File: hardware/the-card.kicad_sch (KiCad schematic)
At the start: 75 parts, among them J1 TYPE-C-31-M-12, J2 FH12-24S-0.5SH(55), J3 S2B-PH-SM4-TB(LF)(SN), Q1 SI2301CDS-T1-GE3, Q2 SI2301CDS-T1-GE3, Q3 SI1308EDL-T1-GE3, SW1 TS-1187A-B-A-B, SW2 TS-1187A-B-A-B, SW3 TS-1187A-B-A-B, SW4 TS-1187A-B-A-B, U1 ESP32-S3-WROOM-1-N16R8, U10 USBLC6-2SC6, U2 ST25DV04KC-IE8S3, U3 LSM6DSOTR, U4 SHT40-BD1B-R2, U5 MAX17048G+T10, U6 TP4056_C382139, U7 DW01A_C18164398, U8 8205A, U9 ME6211C33M5G-N

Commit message: feat(hardware): annotate passive relationships
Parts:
- C1: Function (none) -> MCU high-frequency supply decoupling; Related To (none) -> U1 3V3
- C10: Function (none) -> Fuel-gauge supply decoupling; Related To (none) -> U5 CELL/VDD
- C11: Function (none) -> NFC supply decoupling; Related To (none) -> U2 VCC
- C12: Function (none) -> IMU high-frequency supply decoupling; Related To (none) -> U3 VDD/VDDIO
- C13: Function (none) -> IMU local bulk capacitance; Related To (none) -> U3 VDD/VDDIO / +3V3
- C14: Function (none) -> Humidity-sensor supply decoupling; Related To (none) -> U4 VDD
- C15: Function (none) -> Addressable-LED supply decoupling; Related To (none) -> D1 VDD / AUX_3V3
- C16: Function (none) -> UP-button hardware debounce; Related To (none) -> SW1 / U1 IO4
- C17: Function (none) -> DOWN-button hardware debounce; Related To (none) -> SW2 / U1 IO5
- C18: Function (none) -> SELECT-button hardware debounce; Related To (none) -> SW3 / U1 IO6
- C19: Function (none) -> MENU-button hardware debounce; Related To (none) -> SW4 / U1 IO7
- C2: Function (none) -> MCU local bulk capacitance; Related To (none) -> U1 3V3 / +3V3
- C20: Function (none) -> E-paper switched-input bulk capacitance; Related To (none) -> J2 VCI / e-paper boost
- C21: Function (none) -> E-paper boost charge-pump capacitor; Related To (none) -> J2 / Q3 / EPD_PUMP
- C22: Function (none) -> E-paper internal core-regulator bypass; Related To (none) -> J2 VDD
- C23: Function (none) -> E-paper positive source-rail reservoir; Related To (none) -> J2 VSH2
- C24: Function (none) -> E-paper positive source-rail reservoir; Related To (none) -> J2 VSH1
- C25: Function (none) -> E-paper positive gate-rail reservoir; Related To (none) -> J2 VGH
- C26: Function (none) -> E-paper negative source-rail reservoir; Related To (none) -> J2 VSL
- C27: Function (none) -> E-paper negative gate-rail reservoir; Related To (none) -> J2 VGL
- C28: Function (none) -> E-paper common-electrode rail reservoir; Related To (none) -> J2 VCOM
- C3: Function (none) -> MCU reset and startup timing; Related To (none) -> U1 EN
- C4: Function (none) -> Battery measurement low-pass filter; Related To (none) -> U1 IO1 / battery ADC
- C5: Function (none) -> USB input bulk capacitance; Related To (none) -> J1 / U10 / U6 VBUS
- C6: Function (none) -> Charger output and battery-rail bulk capacitance; Related To (none) -> U6 BAT / +BAT
- C7: Function (none) -> Battery-protection supply decoupling; Related To (none) -> U7 VDD / BAT_NEG
- C8: Function (none) -> LDO input bypass and stability capacitance; Related To (none) -> U9 VIN
- C9: Function (none) -> LDO output stability capacitance; Related To (none) -> U9 VOUT
- R1: Function (none) -> MCU enable pull-up to +3V3; Related To (none) -> U1 EN
- R10: Function (none) -> Battery-protection pack-negative sense resistor; Related To (none) -> U7 VM / GND
- R11: Function (none) -> AUX rail P-MOSFET gate pull-up (default off); Related To (none) -> Q1 / U1 IO47
- R12: Function (none) -> E-paper P-MOSFET gate pull-up (default off); Related To (none) -> Q2 / U1 IO16
- R13: Function (none) -> Shared I2C clock pull-up; Related To (none) -> I2C_SCL / U1-U5
- R14: Function (none) -> Shared I2C data pull-up; Related To (none) -> I2C_SDA / U1-U5
- R15: Function (none) -> E-paper boost MOSFET gate pull-down; Related To (none) -> J2 GDR / Q3
- R16: Function (none) -> E-paper boost current-sense resistor; Related To (none) -> J2 RESE / Q3
- R2: Function (none) -> MCU boot-strap pull-up to +3V3; Related To (none) -> U1 IO0
- R3: Function (none) -> Battery ADC divider, upper leg; Related To (none) -> U1 IO1 / +BAT
- R4: Function (none) -> Battery ADC divider, lower leg; Related To (none) -> U1 IO1 / GND
- R5: Function (none) -> USB-C sink configuration pull-down; Related To (none) -> J1 CC1
- R6: Function (none) -> USB-C sink configuration pull-down; Related To (none) -> J1 CC2
- R7: Function (none) -> TP4056 charge-current programming (~500mA); Related To (none) -> U6 PROG
- R8: Function (none) -> Open-drain charge-status pull-up; Related To (none) -> U6 CHRG / U1 IO15
- R9: Function (none) -> Battery-protection supply feed resistor; Related To (none) -> U7 VDD / +BAT
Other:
- note added: "C1/C2 -> U1: 3V3 bypass + bulk; R1/C3 -> U1 EN: pull-up + startup timing"
- note added: "C11 -> U2: NFC bypass; R13/R14 -> I2C bus U1-U5: SCL/SDA pull-ups"
- note added: "C12/C13 -> U3: IMU bypass + bulk; C14 -> U4: sensor bypass"
- note added: "C15 -> D1: LED supply bypass"
- note added: "C16-C19 -> SW1-SW4/U1: button debounce"
- note added: "C20 -> J2 VCI: input bulk; C21 -> J2/Q3: boost pump capacitor"
- note added: "C22-C28 -> J2: core, source, gate, and VCOM rail reservoirs"
- note added: "C5 -> J1/U10/U6: USB input bulk; R5/R6 -> J1: CC1/CC2 sink pull-downs"
- note added: "C8/C9 -> U9: LDO input/output stability; C10 -> U5: fuel-gauge bypass"
- note added: "R11 -> Q1/U1: AUX gate pull-up; R12 -> Q2/U1: e-paper gate pull-up"
- note added: "R15 -> J2/Q3: boost gate pull-down; R16 -> J2/Q3: current sense"
- note added: "R2 -> U1 IO0: boot pull-up; R3/R4/C4 -> U1 IO1: battery divider + filter"
- note added: "R7 -> U6: charge-current set; R8 -> U6/U1: CHRG pull-up; C6 -> U6: BAT bulk"
- note added: "R9/R10/C7 -> U7/U8: protection supply, sense, and bypass"

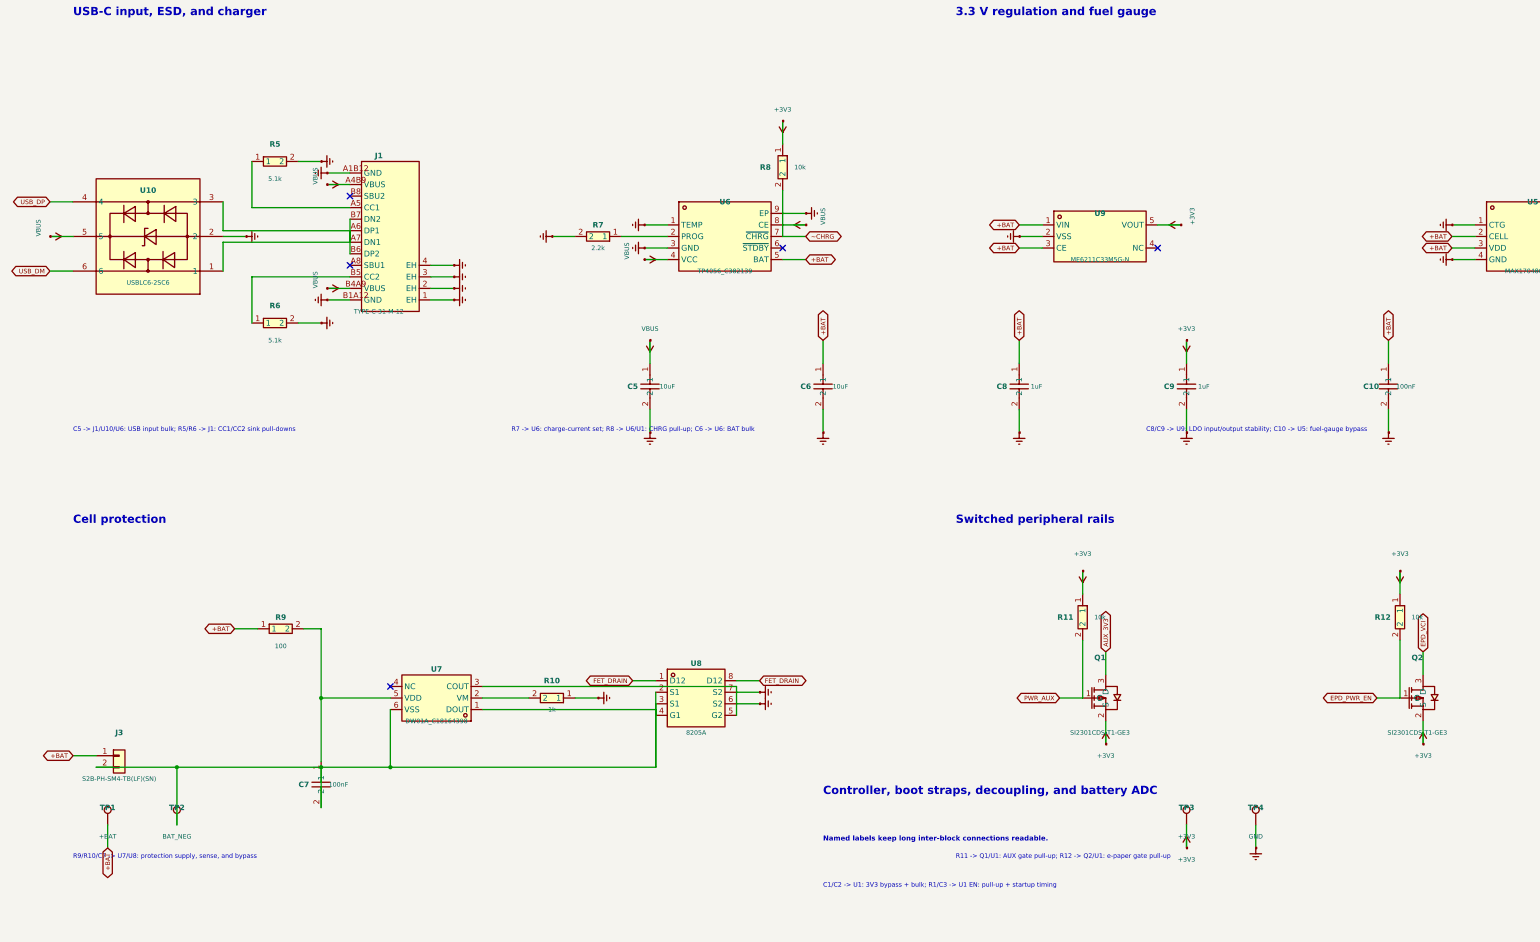
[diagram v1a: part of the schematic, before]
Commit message: feat(hardware): group schematic support passives
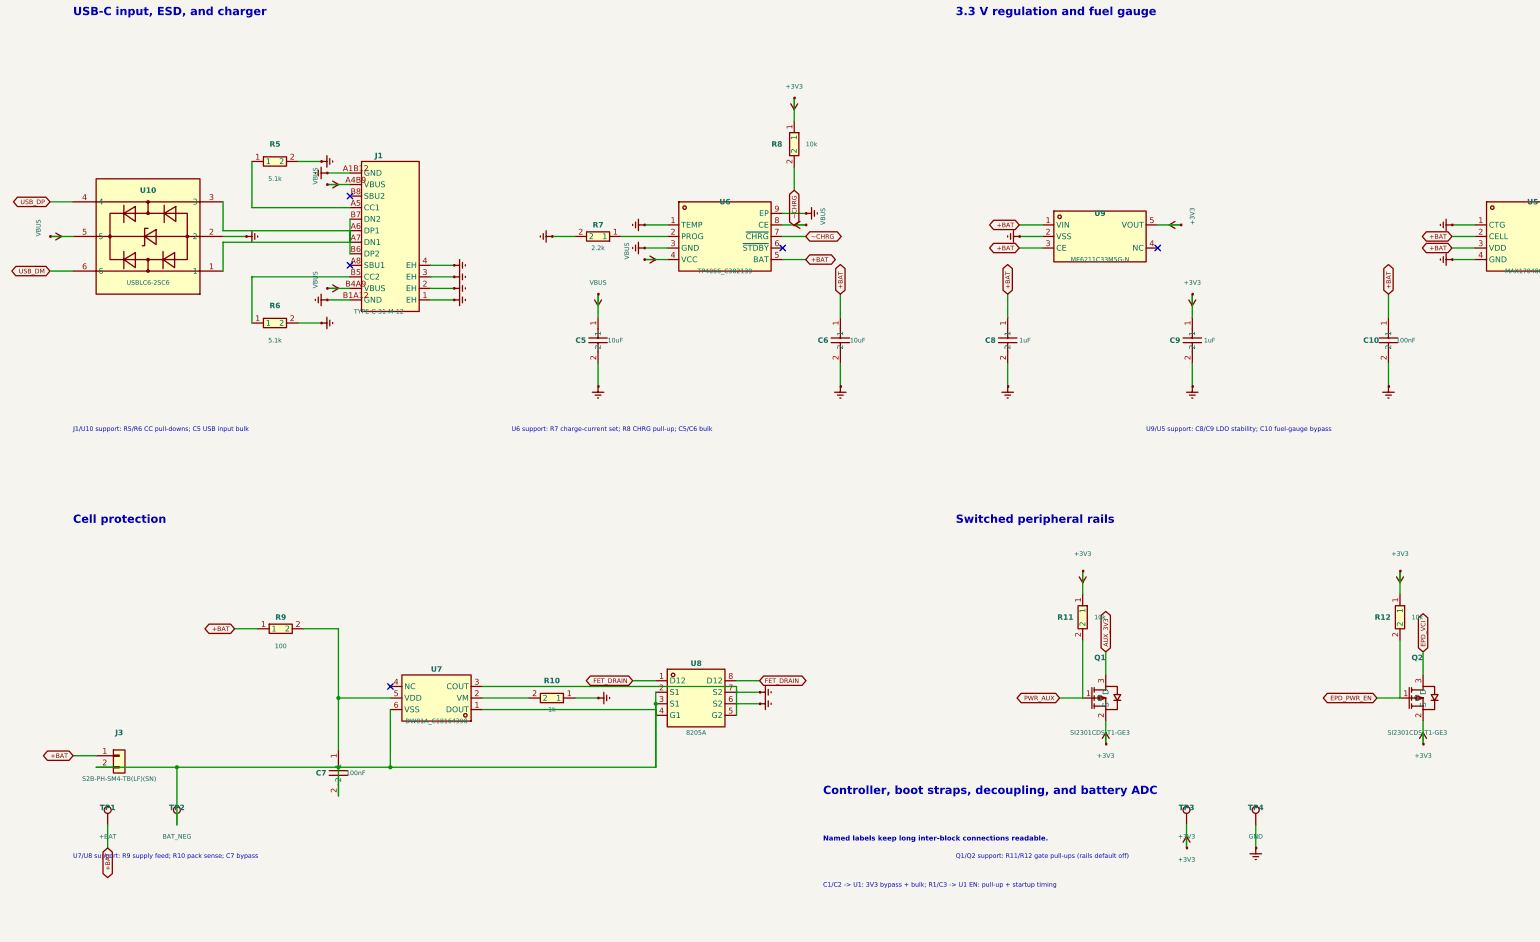
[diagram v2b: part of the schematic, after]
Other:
- note added: "J1/U10 support: R5/R6 CC pull-downs; C5 USB input bulk"
- note added: "Q1/Q2 support: R11/R12 gate pull-ups (rails default off)"
- note added: "U6 support: R7 charge-current set; R8 CHRG pull-up; C5/C6 bulk"
- note added: "U7/U8 support: R9 supply feed; R10 pack sense; C7 bypass"
- note added: "U9/U5 support: C8/C9 LDO stability; C10 fuel-gauge bypass"
- note removed: "C5 -> J1/U10/U6: USB input bulk; R5/R6 -> J1: CC1/CC2 sink pull-downs"
- note removed: "C8/C9 -> U9: LDO input/output stability; C10 -> U5: fuel-gauge bypass"
- note removed: "R11 -> Q1/U1: AUX gate pull-up; R12 -> Q2/U1: e-paper gate pull-up"
- note removed: "R7 -> U6: charge-current set; R8 -> U6/U1: CHRG pull-up; C6 -> U6: BAT bulk"
- note removed: "R9/R10/C7 -> U7/U8: protection supply, sense, and bypass"
- moved on the sheet: C10, C5, C6, C7, C8, C9, R8

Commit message: refactor(hardware): collapse local schematic labels
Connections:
- net MCU_BOOT: no longer names the net of R2.2, TP6.1, U1.27 (IO0)
- net MCU_EN: no longer names the net of C3.1, R1.2, TP5.1, U1.3 (EN)
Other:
- moved on the sheet: R8
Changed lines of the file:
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@@
 	(symbol
 		(lib_id "passives:0402WGF1002TCE")
-		(at 173.99 43.18 270)
+		(at 187.96 63.5 180)
 		(unit 1)
 		(exclude_from_sim no)
@@
 		(dnp no)
 		(property "Reference" "R8"
-			(at 170.18 43.18 90)
+			(at 187.96 60.96 0)
 			(effects (font (size 1.2 1.2) (bold yes)))
 		)
 		(property "Value" "10k"
-			(at 177.8 43.18 90)
+			(at 187.96 66.04 0)
 			(effects (font (size 1 1)))
 		)
 		(property "Footprint" "Resistor_SMD:R_0402_1005Metric"
-			(at 173.99 43.18 0)
+			(at 187.96 63.5 0)
 			(effects (font (size 1 1)) (hide yes))
 		)
 		(property "Datasheet" "https://lcsc.com/product-detail/Chip-Resistor-Surface-Mount-UniOhm_10KR-1002-1_C25744.html"
-			(at 173.99 43.18 0)
+			(at 187.96 63.5 0)
 			(effects (font (size 1 1)) (hide yes))
 		)
 		(property "Function" "Open-drain charge-status pull-up"
-			(at 173.99 43.18 0)
+			(at 187.96 63.5 0)
 			(effects (font (size 1 1)) (hide yes))
 		)
 		(property "Related To" "U6 CHRG / U1 IO15"
-			(at 173.99 43.18 0)
+			(at 187.96 63.5 0)
 			(effects (font (size 1 1)) (hide yes))
 		)
@@
 	)
 	(wire
-		(pts (xy 173.99 38.1) (xy 173.99 33.02))
+		(pts (xy 193.04 63.5) (xy 198.12 63.5))
 		(stroke (width 0) (type default))
 	)
 	(global_label "+3V3"
 		(shape bidirectional)
-		(at 173.99 33.02 0)
+		(at 198.12 63.5 0)
 		(effects (font (size 0.01 0.01)) (hide yes))
 	)
 	(symbol
 		(lib_id "power:+3V3")
-		(at 173.99 33.02 180)
+		(at 198.12 63.5 90)
 		(unit 1)
 		(exclude_from_sim no)
@@
 		(dnp no)
 		(property "Reference" "#PWR0101"
-			(at 173.99 33.02 0)
+			(at 198.12 63.5 0)
 			(effects (font (size 1 1)) (hide yes))
 		)
 		(property "Value" "+3V3"
-			(at 173.99 30.48 0)
-			(effects (font (size 1 1)))
+			(at 200.66 63.5 0)
+			(effects (font (size 1 1)) (justify left))
 		)
-		(property "Footprint" "" (at 173.99 33.02 0) (effects (font (size 1 1)) (hide yes)))
-		(property "Datasheet" "" (at 173.99 33.02 0) (effects (font (size 1 1)) (hide yes)))
+		(property "Footprint" "" (at 198.12 63.5 0) (effects (font (size 1 1)) (hide yes)))
+		(property "Datasheet" "" (at 198.12 63.5 0) (effects (font (size 1 1)) (hide yes)))
 		(pin "1")
 		(instances (project "the-card" (path "/46c60ea8-8fa1-58ec-bd53-17ce943b4943" (reference "#PWR0101") (unit 1))))
@@
 	)
 	(wire
-		(pts (xy 171.45 63.5) (xy 176.53 63.5))
+		(pts (xy 171.45 63.5) (xy 182.88 63.5))
 		(stroke (width 0) (type default))
 	)
-	(global_label "~CHRG"
-		(shape bidirectional)
-		(at 176.53 63.5 0)
-		(effects (font (size 1 1)) (justify left))
-	)
 	(wire
-		(pts (xy 173.99 48.26) (xy 173.99 53.34))
+		(pts (xy 171.45 63.5) (xy 176.53 63.5))
 		(stroke (width 0) (type default))
 	)
 	(global_label "~CHRG"
 		(shape bidirectional)
-		(at 173.99 53.34 270)
-		(effects (font (size 1 1)) (justify right))
+		(at 176.53 63.5 0)
+		(effects (font (size 1 1)) (justify left))
 	)
 	(text "Controller, boot straps, decoupling, and battery ADC"
@@
 	)
 	(wire
-		(pts (xy 332.74 281.94) (xy 339.09 281.94))
+		(pts (xy 332.74 281.94) (xy 365.76 281.94))
 		(stroke (width 0) (type default))
 	)
-	(global_label "MCU_BOOT"
-		(shape bidirectional)
-		(at 339.09 281.94 0)
-		(effects (font (size 0.8 0.8)) (justify left))
-	)
 	(wire
-		(pts (xy 353.06 280.67) (xy 353.06 285.75))
+		(pts (xy 353.06 280.67) (xy 353.06 281.94))
 		(stroke (width 0) (type default))
 	)
-	(global_label "MCU_BOOT"
-		(shape bidirectional)
-		(at 353.06 285.75 270)
-		(effects (font (size 1 1)) (justify right))
+	(junction
+		(at 353.06 281.94)
+		(diameter 0)
+		(color 0 0 0 0)
 	)
 	(wire
-		(pts (xy 365.76 300.99) (xy 365.76 306.07))
+		(pts (xy 365.76 300.99) (xy 365.76 281.94))
 		(stroke (width 0) (type default))
 	)
-	(global_label "MCU_BOOT"
-		(shape bidirectional)
-		(at 365.76 306.07 270)
-		(effects (font (size 1 1)) (justify right))
-	)
 	(wire
-		(pts (xy 289.56 254) (xy 283.21 254))
+		(pts (xy 275.59 250.19) (xy 275.59 300.99))
 		(stroke (width 0) (type default))
 	)
-	(global_label "MCU_EN"
-		(shape bidirectional)
-		(at 283.21 254 180)
-		(effects (font (size 0.8 0.8)) (justify right))
-	)
 	(wire
-		(pts (xy 275.59 250.19) (xy 275.59 255.27))
+		(pts (xy 289.56 254) (xy 275.59 254))
 		(stroke (width 0) (type default))
 	)
-	(global_label "MCU_EN"
-		(shape bidirectional)
-		(at 275.59 255.27 270)
-		(effects (font (size 1 1)) (justify right))
+	(junction
+		(at 275.59 254)
+		(diameter 0)
+		(color 0 0 0 0)
 	)
 	(wire
-		(pts (xy 250.19 255.27) (xy 250.19 250.19))
+		(pts (xy 250.19 255.27) (xy 275.59 255.27))
 		(stroke (width 0) (type default))
 	)
-	(global_label "MCU_EN"
-		(shape bidirectional)
-		(at 250.19 250.19 90)
-		(effects (font (size 1 1)) (justify left))
+	(junction
+		(at 275.59 255.27)
+		(diameter 0)
+		(color 0 0 0 0)
 	)
 	(wire
-		(pts (xy 254 300.99) (xy 254 306.07))
+		(pts (xy 254 300.99) (xy 275.59 300.99))
 		(stroke (width 0) (type default))
 	)
-	(global_label "MCU_EN"
-		(shape bidirectional)
-		(at 254 306.07 270)
-		(effects (font (size 1 1)) (justify right))
-	)
 	(wire
 		(pts (xy 332.74 252.73) (xy 365.76 252.73))
@@
 	)
 	(wire
-		(pts (xy 433.07 298.45) (xy 427.99 298.45))
+		(pts (xy 433.07 298.45) (xy 425.45 298.45))
 		(stroke (width 0) (type default))
 	)
-	(global_label "EPD_GDR"
-		(shape bidirectional)
-		(at 427.99 298.45 180)
-		(effects (font (size 1 1)) (justify right))
+	(wire
+		(pts (xy 425.45 298.45) (xy 425.45 325.12))
+		(stroke (width 0) (type default))
 	)
 	(wire
-		(pts (xy 425.45 325.12) (xy 425.45 320.04))
+		(pts (xy 433.07 298.45) (xy 427.99 298.45))
 		(stroke (width 0) (type default))
 	)
 	(global_label "EPD_GDR"
 		(shape bidirectional)
-		(at 425.45 320.04 90)
-		(effects (font (size 1 1)) (justify left))
+		(at 427.99 298.45 180)
+		(effects (font (size 1 1)) (justify right))
 	)
 	(wire
@@
 	)
 	(wire
-		(pts (xy 440.69 303.53) (xy 440.69 308.61))
+		(pts (xy 440.69 303.53) (xy 450.85 303.53))
 		(stroke (width 0) (type default))
 	)
-	(global_label "EPD_RESE"
-		(shape bidirectional)
-		(at 440.69 308.61 270)
-		(effects (font (size 1 1)) (justify right))
+	(wire
+		(pts (xy 450.85 303.53) (xy 450.85 325.12))
+		(stroke (width 0) (type default))
 	)
 	(wire
-		(pts (xy 450.85 325.12) (xy 450.85 320.04))
+		(pts (xy 440.69 303.53) (xy 440.69 308.61))
 		(stroke (width 0) (type default))
 	)
 	(global_label "EPD_RESE"
 		(shape bidirectional)
-		(at 450.85 320.04 90)
-		(effects (font (size 1 1)) (justify left))
+		(at 440.69 308.61 270)
+		(effects (font (size 1 1)) (justify right))
 	)
 	(wire
@@
 	)
 	(wire
-		(pts (xy 472.44 279.4) (xy 467.36 279.4))
+		(pts (xy 472.44 279.4) (xy 502.92 279.4))
 		(stroke (width 0) (type default))
 	)
-	(global_label "EPD_VGH"
-		(shape bidirectional)
-		(at 467.36 279.4 180)
-		(effects (font (size 1 1)) (justify right))
+	(wire
+		(pts (xy 502.92 279.4) (xy 502.92 264.16))
+		(stroke (width 0) (type default))
 	)
 	(wire
-		(pts (xy 502.92 264.16) (xy 497.84 264.16))
+		(pts (xy 472.44 279.4) (xy 467.36 279.4))
 		(stroke (width 0) (type default))
 	)
 	(global_label "EPD_VGH"
 		(shape bidirectional)
-		(at 497.84 264.16 180)
+		(at 467.36 279.4 180)
 		(effects (font (size 1 1)) (justify right))
 	)

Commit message: fix(hardware): clarify schematic routing
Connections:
- net at C7.2, J3.2 (Pin_2), TP2.1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: no longer U7.1 (DOUT), U8.4 (G1)
- new net: U7.1 (DOUT), U8.4 (G1)
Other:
- moved on the sheet: C16, C17, C18, C19, C21, C7, R11, R12, U8

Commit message: refactor(hardware): improve schematic placement
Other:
- note added: "C11 -> U2: NFC bypass"
- note added: "C12/C13 -> U3: IMU bypass + bulk"
- note added: "C14 -> U4: environmental-sensor bypass"
- note added: "R13/R14 -> I2C bus U1-U5: SCL/SDA pull-ups"
- note removed: "C11 -> U2: NFC bypass; R13/R14 -> I2C bus U1-U5: SCL/SDA pull-ups"
- note removed: "C12/C13 -> U3: IMU bypass + bulk; C14 -> U4: sensor bypass"
- moved on the sheet: C10, C12, C13, C14, C22, C24, C25, C26, C27, C28, C5, C6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

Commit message: fix(hardware): improve schematic section spacing
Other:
- moved on the sheet: C1, C19, C2, C20, C25, C3, C4, D4, J2, R1, R2, R3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
